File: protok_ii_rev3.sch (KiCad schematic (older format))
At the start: 196 parts, among them U1 proton_c

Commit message: update schematic
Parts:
- removed Decoder1, Decoder2: 74HC238, Package_SO:SOIC-16_3.9x9.9mm_P1.27mm, symbol 74xx_IEEE:74HC238
- removed Rotary2: EC21A1540401, SamacSys_Parts:EC21A1540401, symbol SamacSys_Parts:EC21A1540401
- removed Rotary_SW1: B3F-1000, digikey-footprints:Switch_Tactile_THT_B3F-1xxx, symbol dk_Tactile-Switches:B3F-1000
- added C1: 100nF, Capacitor_SMD:C_0402_1005Metric, symbol Device:C
- added J1: Conn_01x04_Male, Connector_PinHeader_2.54mm:PinHeader_1x04_P2.54mm_Horizontal, symbol Connector:Conn_01x04_Male
- added J2: Conn_01x04_Male, my_lib:MKI2C-2V, symbol Connector:Conn_01x04_Male
- added R5, R6: 10K, Resistor_SMD:R_0402_1005Metric, symbol Device:R
- added S1, S2: 1825910-6, digikey-footprints:Switch_Tactile_THT_6x6mm, symbol dk_Tactile-Switches:1825910-6
- added SW1: Rotary_Encoder, my_lib:EC35A1520402, symbol Device:Rotary_Encoder
- added U2: MCP23017_SO, Package_SO:SOIC-28W_7.5x17.9mm_P1.27mm, symbol Interface_Expansion:MCP23017_SO
- R1, R2, R3, R4: value 5.1k -> 10K; LCSC (none) -> C25744
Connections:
- net labels added: A1, A2, A3, B1, B2, B3, DFU, J_EN, MISO, MOSI, RST, RX, SCL, SCLK, SDA, TX
- net labels removed: ColAddr0, ColAddr1, ColAddr2, ColHiEn, ColLoEn
- wire segments 353 -> 403

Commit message: update component
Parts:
- added J3: Conn_01x02_Male, Connector_PinHeader_2.54mm:PinHeader_1x02_P2.54mm_Horizontal, symbol Connector:Conn_01x02_Male
- added J4: Conn_01x07_Male, Connector_PinHeader_2.54mm:PinHeader_1x07_P2.54mm_Horizontal, symbol Connector:Conn_01x07_Male
- added R7, R8: 10K, Resistor_SMD:R_0402_1005Metric, symbol Device:R
- D1, D10, D11, D12, D13, D14, D15, D16, D17, D18, D19, D2, D20, D21, D22, D23, D24, D25, D26, D27, D28, D29, D3, D30, D31, D32, D33, D34, D35, D36, D37, D38, D39, D4, D40, D41, D42, D43, D44, D45, D46, D47, D48, D49, D5, D50, D51, D52, D53, D54, D55, D56, D57, D58, D59, D6, D60, D61, D62, D63, D64, D65, D66, D67, D68, D69, D7, D70, D71, D72, D73, D74, D75, D76, D77, D78, D79, D8, D80, D81, D82, D83, D84, D85, D86, D87, D88, D89, D9, D90, D91, D92, D93: LCSC (none) -> C81598
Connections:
- net +3V3: now also R7.2, R8.2
- net A1: now also U1.A1 (PA1), J4.2 (Pin_2)
- net A2: now also U1.A2 (PA2), J4.1 (Pin_1)
- net Col0: no longer U1.A8 (PA8)
- net Col1: no longer U1.A15 (PA15)
- net Col2: no longer U1.B10 (PB10)
- net Col3: no longer U1.B11 (PB11)
- net Col4: no longer U1.B12 (PB12)
- net Col5: no longer U1.A14 (PA14/SWCLK)
- net Col6: no longer U1.A13 (PA13/SWDIO)
- net DFU: now also S1.2
- net GND: now also S1.4, S2.4
- net MISO: now also J4.6 (Pin_6)
- net MOSI: now also J4.7 (Pin_7)
- net RST: now also S2.2
- net RX: now also J3.2 (Pin_2)
- net Row0: now also U1.A8 (PA8)
- net Row1: now also U1.A15 (PA15)
- net Row2: now also U1.B10 (PB10)
- net Row3: now also U1.B11 (PB11)
- net Row4: now also U1.B12 (PB12)
- net Row5: now also U1.A14 (PA14/SWCLK)
- net Row6: now also U1.A13 (PA13/SWDIO)
- net SCLK: now also J4.5 (Pin_5)
- net TX: now also J3.1 (Pin_1)
- net A0: now reaches U1.A0 (PA0)
- net A0: now also J4.3 (Pin_3)
- net B8: now reaches U1.B8 (PB8)
- net B8: now also J4.4 (Pin_4)
- net at U2.19 (INTB): now also R7.1
- net at U2.20 (INTA): now also R8.1
- no-connect marks 0 -> 12
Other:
- moved on the sheet: J1, J2, S1, S2, U1

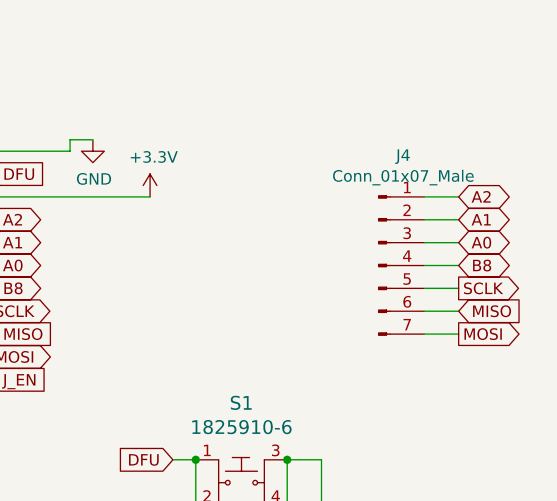
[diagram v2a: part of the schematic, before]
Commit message: update schematic
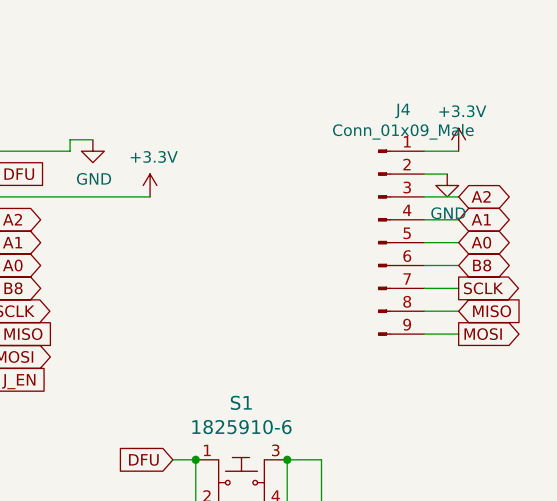
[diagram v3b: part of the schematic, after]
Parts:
- removed J4: Conn_01x07_Male, Connector_PinHeader_2.54mm:PinHeader_1x07_P2.54mm_Horizontal, symbol Connector:Conn_01x07_Male
- added J4: Conn_01x09_Male, Connector_PinHeader_2.54mm:PinHeader_1x09_P2.54mm_Horizontal, symbol Connector:Conn_01x09_Male
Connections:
- net +3V3: now also J4.1 (Pin_1)
- net A0: now also J4.5 (Pin_5)
- net A1: now also J4.4 (Pin_4)
- net A2: now also J4.3 (Pin_3)
- net B8: now also J4.6 (Pin_6)
- net GND: now also J4.2 (Pin_2)
- net MISO: now also J4.8 (Pin_8)
- net MOSI: now also J4.9 (Pin_9)
- net SCLK: now also J4.7 (Pin_7)
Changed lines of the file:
@@
-$EndComp
-$Comp
-L power:+3.3V #PWR01
-U 1 1 61517FDC
-P 10650 6550
-F 0 "#PWR01" H 10650 6400 50  0001 C CNN
-F 1 "+3.3V" H 10665 6723 50  0000 C CNN
-F 2 "" H 10650 6550 50  0001 C CNN
-F 3 "" H 10650 6550 50  0001 C CNN
-	1    10650 6550
-	1    0    0    -1
 $EndComp
 $Comp
@@
 $EndComp
 $Comp
-L power:+3.3V #PWR0103
-U 1 1 61AA6C41
-P 2400 7600
-F 0 "#PWR0103" H 2400 7450 50  0001 C CNN
-F 1 "+3.3V" H 2415 7773 50  0000 C CNN
-F 2 "" H 2400 7600 50  0001 C CNN
-F 3 "" H 2400 7600 50  0001 C CNN
-	1    2400 7600
-	1    0    0    -1
-$EndComp
-$Comp
 L Connector:Conn_01x04_Male J2
 U 1 1 61B0DBF7
@@
 	1    0    0    -1
 $EndComp
-$Comp
-L Connector:Conn_01x07_Male J4
-U 1 1 613C36E4
-P 14650 1850
-F 0 "J4" H 14758 2331 50  0000 C CNN
-F 1 "Conn_01x07_Male" H 14758 2240 50  0000 C CNN
-F 2 "Connector_PinHeader_2.54mm:PinHeader_1x07_P2.54mm_Horizontal" H 14650 1850 50  0001 C CNN
-F 3 "~" H 14650 1850 50  0001 C CNN
-	1    14650 1850
-	1    0    0    -1
-$EndComp
 Text GLabel 15000 2150 2    50   Output ~ 0
 MOSI
@@
 Wire Wire Line
 	12850 1550 13650 1550
+Wire Wire Line
+	10650 6600 10650 6550
+Connection ~ 10650 6600
 $Comp
 L power:+3.3V #PWR0102
-U 1 1 61AD8F09
+U 1 1 614168C2
+P 2400 7600
+F 0 "#PWR0102" H 2400 7450 50  0001 C CNN
+F 1 "+3.3V" H 2415 7773 50  0000 C CNN
+F 2 "" H 2400 7600 50  0001 C CNN
+F 3 "" H 2400 7600 50  0001 C CNN
+	1    2400 7600
+	1    0    0    -1
+$EndComp
+$Comp
+L power:+3.3V #PWR0103
+U 1 1 61418FF0
 P 13650 1550
-F 0 "#PWR0102" H 13650 1400 50  0001 C CNN
+F 0 "#PWR0103" H 13650 1400 50  0001 C CNN
 F 1 "+3.3V" H 13665 1723 50  0000 C CNN
 F 2 "" H 13650 1550 50  0001 C CNN
@@
 	1    0    0    -1
 $EndComp
-Wire Wire Line
-	10650 6600 10650 6550
-Connection ~ 10650 6600
+$Comp
+L power:+3.3V #PWR0107
+U 1 1 6141B344
+P 10650 6550
+F 0 "#PWR0107" H 10650 6400 50  0001 C CNN
+F 1 "+3.3V" H 10665 6723 50  0000 C CNN
+F 2 "" H 10650 6550 50  0001 C CNN
+F 3 "" H 10650 6550 50  0001 C CNN
+	1    10650 6550
+	1    0    0    -1
+$EndComp
+$Comp
+L Connector:Conn_01x09_Male J4
+U 1 1 6141F571
+P 14650 1750
+F 0 "J4" H 14758 2331 50  0000 C CNN
+F 1 "Conn_01x09_Male" H 14758 2240 50  0000 C CNN
+F 2 "Connector_PinHeader_2.54mm:PinHeader_1x09_P2.54mm_Horizontal" H 14650 1750 50  0001 C CNN
+F 3 "~" H 14650 1750 50  0001 C CNN
+	1    14650 1750
+	1    0    0    -1
+$EndComp
+$Comp
+L power:+3.3V #PWR0108
+U 1 1 6147DF30
+P 15000 1350
+F 0 "#PWR0108" H 15000 1200 50  0001 C CNN
+F 1 "+3.3V" H 15015 1523 50  0000 C CNN
+F 2 "" H 15000 1350 50  0001 C CNN
+F 3 "" H 15000 1350 50  0001 C CNN
+	1    15000 1350
+	1    0    0    -1
+$EndComp
+$Comp
+L power:GND #PWR0109
+U 1 1 6148057F
+P 14950 1450
+F 0 "#PWR0109" H 14950 1200 50  0001 C CNN
+F 1 "GND" H 14955 1277 50  0000 C CNN
+F 2 "" H 14950 1450 50  0001 C CNN
+F 3 "" H 14950 1450 50  0001 C CNN
+	1    14950 1450
+	1    0    0    -1
+$EndComp
+Wire Wire Line
+	14850 1450 14950 1450
+Wire Wire Line
+	15000 1350 14850 1350
 $EndSCHEMATC

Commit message: finish pcb
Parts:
- removed J3: Conn_01x02_Male, Connector_PinHeader_2.54mm:PinHeader_1x02_P2.54mm_Horizontal, symbol Connector:Conn_01x02_Male
- removed J4: Conn_01x09_Male, Connector_PinHeader_2.54mm:PinHeader_1x09_P2.54mm_Horizontal, symbol Connector:Conn_01x09_Male
- removed R4, R5, R7, R8: 10K, Resistor_SMD:R_0402_1005Metric, symbol Device:R
- removed S1, S2: 1825910-6, digikey-footprints:Switch_Tactile_THT_6x6mm, symbol dk_Tactile-Switches:1825910-6
- added BZ1: Buzzer, my_lib:AST1109MLTRQ, symbol Device:Buzzer
- added J1: AudioPlug4, my_lib:3.5mm_phone_jack_THT, symbol Connector:AudioPlug4
- added J2: Conn_01x10_Male, Connector_PinHeader_2.54mm:PinHeader_1x10_P2.54mm_Horizontal, symbol Connector:Conn_01x10_Male
- added P1: USB_C_Plug, my_lib:TYPE-C-31-M-04, symbol Connector:USB_C_Plug
- added R3: 5.1K, Resistor_SMD:R_0402_1005Metric, symbol Device:R
- J4: renamed from J2; footprint my_lib:MKI2C-2V -> Connector_PinHeader_2.54mm:PinHeader_1x04_P2.54mm_Horizontal
- renumbered D93 to D1, D9 to D10, D10 to D11, D11 to D12, D12 to D13, D13 to D14, D14 to D15, D15 to D16, D16 to D17, D17 to D18, D18 to D19, D1 to D2, D19 to D20, D20 to D21, D21 to D22, D22 to D23, D23 to D24, D24 to D25, D25 to D26, D26 to D27, D27 to D28, D28 to D29, D2 to D3, D29 to D30, D30 to D31, D31 to D32, D32 to D33, D33 to D34, D34 to D35, D35 to D36, D36 to D37, D37 to D38, D38 to D39, D3 to D4, D39 to D40, D40 to D41, D41 to D42, D42 to D43, D43 to D44, D44 to D45, D45 to D46, D46 to D47, D47 to D48, D48 to D49, D4 to D5, D49 to D50, D50 to D51, D51 to D52, D52 to D53, D53 to D54, D54 to D55, D55 to D56, D56 to D57, D57 to D58, D58 to D59, D5 to D6, D59 to D60, D60 to D61, D61 to D62, D62 to D63, D63 to D64, D64 to D65, D65 to D66, D66 to D67, D67 to D68, D68 to D69, D6 to D7, D69 to D70, D70 to D71, D71 to D72, D72 to D73, D73 to D74, D74 to D75, D75 to D76, D76 to D77, D77 to D78, D78 to D79, D7 to D8, D79 to D80, D80 to D81, D81 to D82, D82 to D83, D83 to D84, D84 to D85, D85 to D86, D86 to D87, D87 to D88, D88 to D89, D8 to D9, D89 to D90, D90 to D91, D91 to D92, D92 to D93, J1 to J3, R3 to R4, R6 to R5
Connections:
- net +3V3: now also J4.2 (Pin_2), J1.S, J2.1 (Pin_1); no longer J4.4 (Pin_4)
- net A0: now also J2.5 (Pin_5)
- net A1: now also U1.B2 (PB2); no longer U1.A1 (PA1), U1.B0 (PB0)
- net A2: now also U1.B4 (PB4); no longer U1.A2 (PA2), U1.B2 (PB2)
- net A3: now also U1.B0 (PB0); no longer U1.B4 (PB4)
- net B1: now also U1.B3 (PB3); no longer U1.B1 (PB1)
- net B2: now also U1.B5 (PB5); no longer U1.B3 (PB3)
- net B3: now also U1.B1 (PB1); no longer U1.B5 (PB5)
- net B8: now also J2.6 (Pin_6)
- net GND: now also BZ1.2 (+), J1.T, J2.2 (Pin_2), P1.A1 (GND), P1.A12 (GND), P1.B1 (GND), P1.B12 (GND), P1.S1 (SHIELD), R3.2
- net J_EN: now also U1.A5 (PA5/SPEAKER2); no longer U1.B9 (PB9)
- net MISO: now also J2.8 (Pin_8)
- net MOSI: now also J2.9 (Pin_9)
- net RX: now also J1.R1
- net SCLK: now also J2.7 (Pin_7)
- net SDA: now also J4.4 (Pin_4); no longer J4.2 (Pin_2)
- net TX: now also J1.R2
- net at U2.20 (INTA): now also R4.1, U2.18 (~RESET~), U2.19 (INTB)
- net VBUS: now reaches U1.5V (VBUS(5V_RAW))
- net VBUS: now also P1.A4 (VBUS), P1.A9 (VBUS), P1.B4 (VBUS), P1.B9 (VBUS)
- net SPK: now reaches U1.A4 (PA4/SPEAKER1)
- net SPK: now also BZ1.1 (-)
- net D+: now reaches U1.D+ (USB-DP)
- net D+: now also P1.A6 (D+)
- net D-: now reaches U1.D- (USB-DM)
- net D-: now also P1.A7 (D-)
- net at R5.1, U2.15 (A0): now also U2.16 (A1), U2.17 (A2)
- net DFU: no longer names the net of U1.DFU
- net RST: no longer names the net of U1.RST (RESET)
- new net: P1.A5 (CC), P1.B5 (VCONN), R3.1
- new net B9: J2.10 (Pin_10), U1.B9 (PB9)
- new net SA1: J2.4 (Pin_4), U1.A1 (PA1)
- new net SA2: J2.3 (Pin_3), U1.A2 (PA2)
- no-connect marks 12 -> 19
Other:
- moved on the sheet: J4

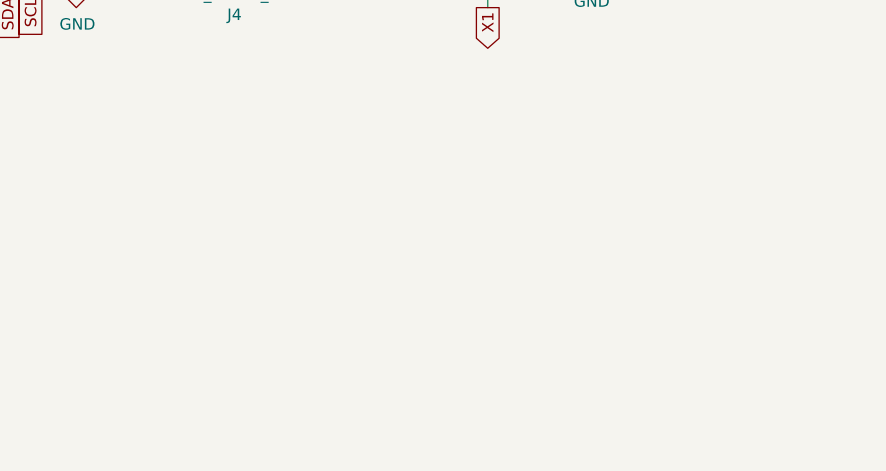
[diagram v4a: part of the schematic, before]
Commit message: final version with eeprom
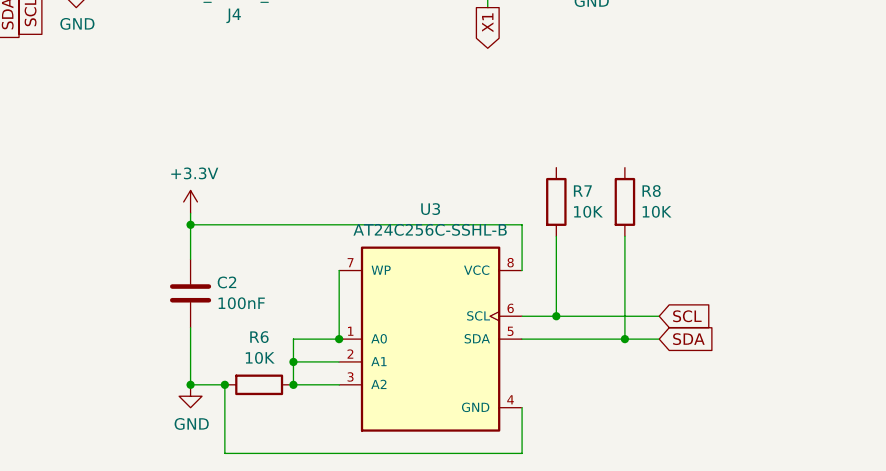
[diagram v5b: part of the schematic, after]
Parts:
- added C2: 100nF, Capacitor_SMD:C_0402_1005Metric, symbol Device:C
- added R6, R7, R8: 10K, Resistor_SMD:R_0402_1005Metric, symbol Device:R
- added U3: AT24C256C-SSHL-B, my_lib:SOIC127P600X175-8N, symbol AT24C256C-SSHL-B:AT24C256C-SSHL-B
- C1, R1, R2, R3, R4, R5: JLC (none) -> 0402
- D1, D10, D11, D12, D13, D14, D15, D16, D17, D18, D19, D2, D20, D21, D22, D23, D24, D25, D26, D27, D28, D29, D3, D30, D31, D32, D33, D34, D35, D36, D37, D38, D39, D4, D40, D41, D42, D43, D44, D45, D46, D47, D48, D49, D5, D50, D51, D52, D53, D54, D55, D56, D57, D58, D59, D6, D60, D61, D62, D63, D64, D65, D66, D67, D68, D69, D7, D70, D71, D72, D73, D74, D75, D76, D77, D78, D79, D8, D80, D81, D82, D83, D84, D85, D86, D87, D88, D89, D9, D90, D91, D92, D93: JLC (none) -> SOD-123
- P1: JLC (none) -> USB-C-SMD
- U2: JLC (none) -> SOIC-28_300mil
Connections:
- net +3V3: now also C2.1, U3.8 (VCC)
- net GND: now also C2.2, R6.2, U3.4 (GND)
- net SCL: now also R7.2, U3.6 (SCL)
- net SDA: now also R8.2, U3.5 (SDA)
- new net: R6.1, U3.1 (A0), U3.2 (A1), U3.3 (A2), U3.7 (WP)
